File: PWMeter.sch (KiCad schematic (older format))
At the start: 20 parts, among them J1 TEST_1P, J2 TEST_1P, J3 TEST_1P, J4 TEST_1P, J5 CONN_01X08, P1 16/9V in, P5 Display, U1 LM317T, U2 MC78M05CDT, U4 Arduino_Nano

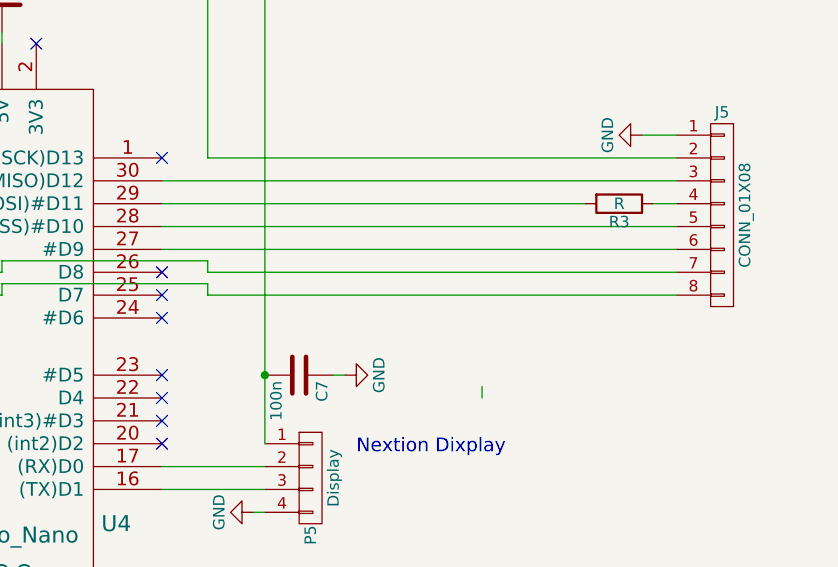
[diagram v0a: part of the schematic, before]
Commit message: minor changes on sylkmask
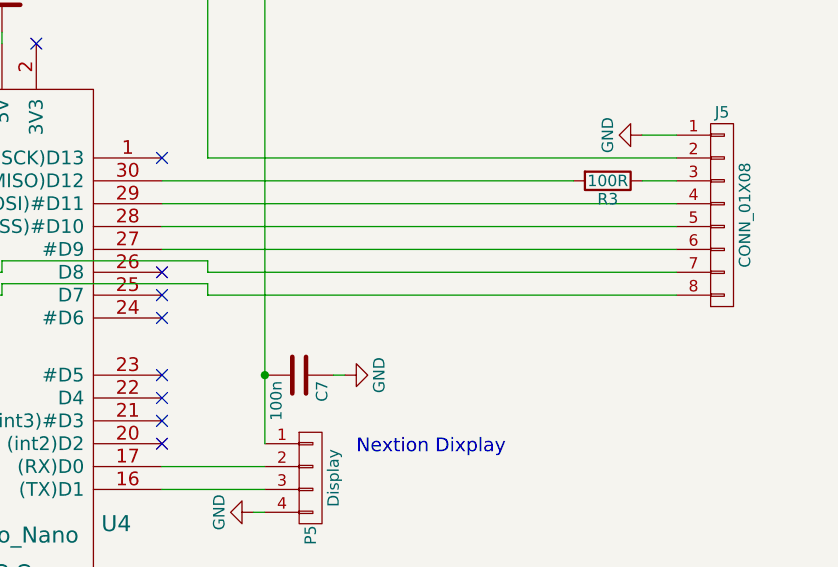
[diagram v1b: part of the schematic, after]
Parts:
- R3: value R -> 100R
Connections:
- wire segments 56 -> 55
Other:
- moved on the sheet: R3
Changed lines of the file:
@@
 EESchema Schematic File Version 2
-LIBS:vfo-do-rescue
 LIBS:power
 LIBS:device
@@
 	7300 5300 7300 5350
 Wire Wire Line
-	8000 3200 10250 3200
-Wire Wire Line
 	8000 3400 10250 3400
 Wire Wire Line
@@
 Wire Wire Line
 	8200 3100 10250 3100
-Wire Wire Line
-	9400 4150 9400 4100
 NoConn ~ 6600 4950
 NoConn ~ 6600 4250
@@
 L R R3
 U 1 1 596B6513
-P 10000 3300
-F 0 "R3" V 10080 3300 50  0000 C CNN
-F 1 "R" V 10000 3300 50  0000 C CNN
-F 2 "Resistors_SMD:R_0805_HandSoldering" V 9930 3300 50  0001 C CNN
-F 3 "" H 10000 3300 50  0001 C CNN
-	1    10000 3300
+P 9950 3200
+F 0 "R3" V 10030 3200 50  0000 C CNN
+F 1 "100R" V 9950 3200 50  0000 C CNN
+F 2 "Resistors_SMD:R_0805_HandSoldering" V 9880 3200 50  0001 C CNN
+F 3 "" H 9950 3200 50  0001 C CNN
+	1    9950 3200
 	0    1    1    0
 $EndComp
 Wire Wire Line
-	10150 3300 10250 3300
-Wire Wire Line
-	9850 3300 8000 3300
+	8000 3300 10250 3300
 NoConn ~ 8000 4350
 NoConn ~ 8000 3800
@@
 Text Notes 8200 7650 0    60   ~ 0
 July 16 2017
+Wire Wire Line
+	10250 3200 10100 3200
+Wire Wire Line
+	9800 3200 8000 3200
 $EndSCHEMATC
